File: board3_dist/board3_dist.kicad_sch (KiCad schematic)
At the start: 9 parts, among them J1 Conn_02x04_Odd_Even, J2 Screw_Terminal_01x02, J3 Screw_Terminal_01x02, J4 Screw_Terminal_01x02, J5 Screw_Terminal_01x02, J6 Conn_01x02, J7 Conn_01x02, J8 Conn_01x02, J9 Conn_01x02

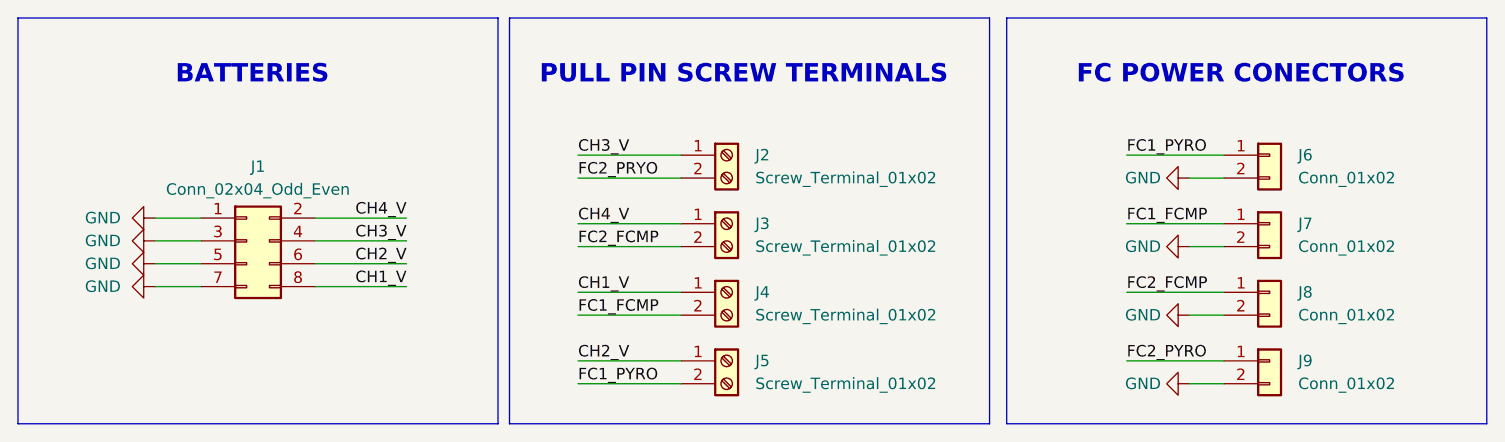
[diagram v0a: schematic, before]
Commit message: connector fixes to the boards - swapped headers with sockets and vice versa. had to adjust the schematics too but no big changes, everything still connected appropriately
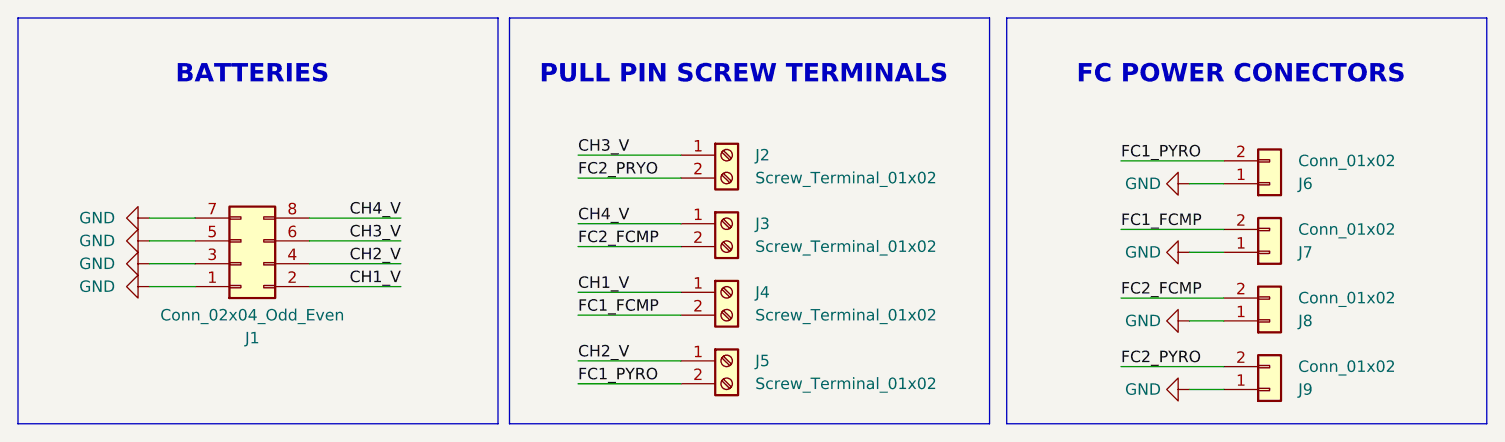
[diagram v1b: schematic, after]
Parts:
- J1: footprint Connector_PinHeader_2.54mm:PinHeader_2x04_P2.54mm_Horizontal -> Connector_PinSocket_2.54mm:PinSocket_2x04_P2.54mm_Horizontal
- J6, J7, J8, J9: footprint Connector_PinHeader_2.54mm:PinHeader_1x02_P2.54mm_Horizontal -> Connector_PinSocket_2.54mm:PinSocket_1x02_P2.54mm_Horizontal
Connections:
- net CH1_V: now also J1.2 (Pin_2); no longer J1.8 (Pin_8)
- net CH2_V: now also J1.4 (Pin_4); no longer J1.6 (Pin_6)
- net CH3_V: now also J1.6 (Pin_6); no longer J1.4 (Pin_4)
- net CH4_V: now also J1.8 (Pin_8); no longer J1.2 (Pin_2)
- net FC1_FCMP: now also J7.2 (Pin_2); no longer J7.1 (Pin_1)
- net FC1_PYRO: now also J6.2 (Pin_2); no longer J6.1 (Pin_1)
- net FC2_FCMP: now also J8.2 (Pin_2); no longer J8.1 (Pin_1)
- net FC2_PYRO: now also J9.2 (Pin_2); no longer J9.1 (Pin_1)
- net GND: now also J6.1 (Pin_1), J7.1 (Pin_1), J8.1 (Pin_1), J9.1 (Pin_1); no longer J6.2 (Pin_2), J7.2 (Pin_2), J8.2 (Pin_2), J9.2 (Pin_2)
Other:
- moved on the sheet: J1, J6, J7, J8, J9
